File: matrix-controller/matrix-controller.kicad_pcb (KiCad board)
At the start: 2 copper layers, 1 part

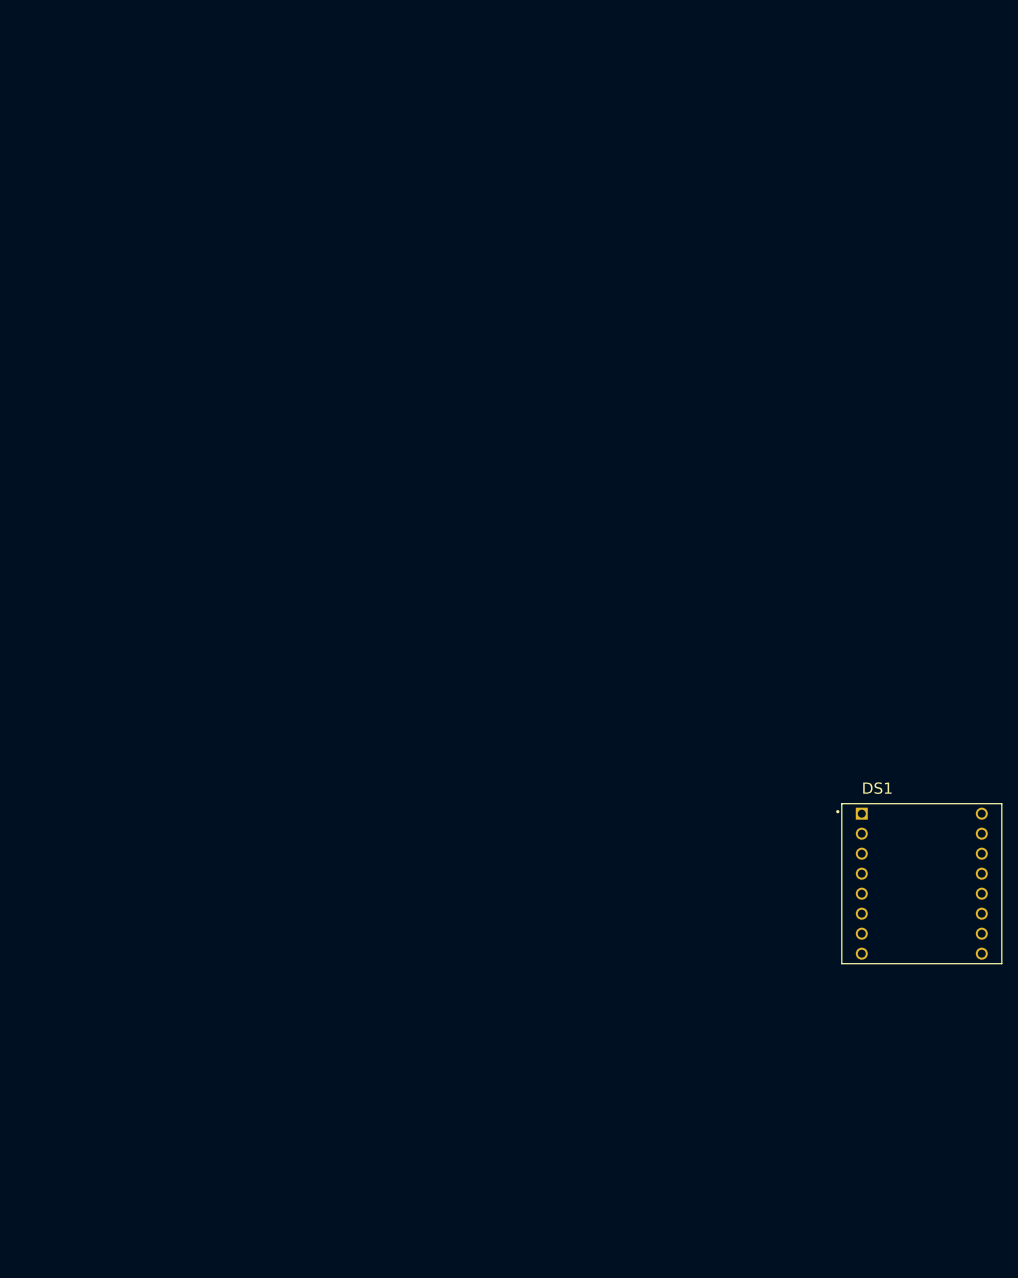
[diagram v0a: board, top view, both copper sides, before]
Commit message: Base of the schematic is done, need to add IMU and regulator and finish the rest of the panels
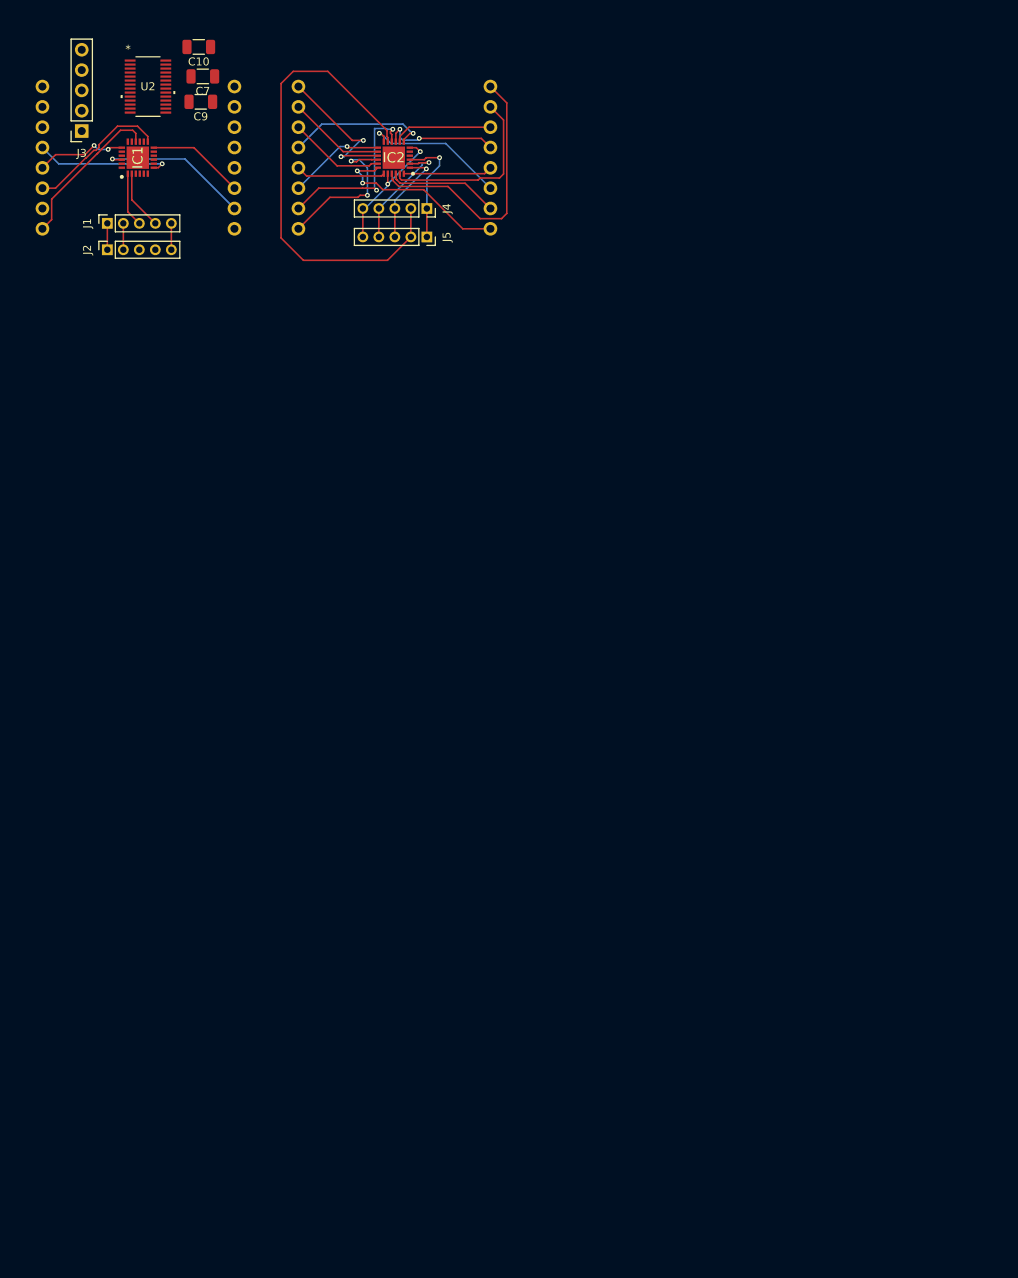
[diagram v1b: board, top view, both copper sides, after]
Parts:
- removed DS1: TA08-81GWA, TA08-81GWA:DISPLAY_TA08-81GWA
- added C10: 0.47uF, Capacitor_SMD:C_1206_3216Metric, F.Cu at (23.6, 2.16)
- added C7: 10uF, Capacitor_SMD:C_1206_3216Metric, F.Cu at (24.1, 5.84)
- added C9: 0.1uF, Capacitor_SMD:C_1206_3216Metric, F.Cu at (23.9, 9.02)
- added IC1: IS31FL3728-QFLS2-TR, IS31FL3728-QFLS2-TR:QFN50P400X400X80-25N-D, F.Cu at (16.0, 16.0)
- added IC2: IS31FL3728-QFLS2-TR, IS31FL3728-QFLS2-TR:QFN50P400X400X80-25N-D, F.Cu at (48.0, 16.0)
- added J1: 1x05_Socket_Front, Connector_PinSocket_2.00mm:PinSocket_1x05_P2.00mm_Vertical, F.Cu at (12.2, 24.2)
- added J2: 1x05_Socket_Back, Connector_PinSocket_2.00mm:PinSocket_1x05_P2.00mm_Vertical, F.Cu at (12.2, 27.5)
- added J3: Conn_01x05_Pin, Connector_PinSocket_2.54mm:PinSocket_1x05_P2.54mm_Vertical, F.Cu at (8.99, 12.7)
- added J4: 1x05_Socket_Front_Input, Connector_PinSocket_2.00mm:PinSocket_1x05_P2.00mm_Vertical, F.Cu at (52.1, 22.4)
- added J5: 1x05_Socket_Left, Connector_PinSocket_2.00mm:PinSocket_1x05_P2.00mm_Vertical, F.Cu at (52.1, 25.9)
- added U1: 1088BS, lib_fp:LED_1088, B.Cu at (32.0, 0.00)
- added U2: XMSM0G3507SDGS28R, footprints:VSSOP28_DGS_TEX, F.Cu at (17.3, 7.11)
- added U3: 1088BS, lib_fp:LED_1088, B.Cu at (64.0, 0.00)
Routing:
- net VCC: track 0.00 -> 63.1 mm
- net /MatrixPlusDriver1/C4: track 0.00 -> 34.2 mm
- net /MatrixPlusDriver1/C2: track 0.00 -> 23.0 mm
- net /MatrixPlusDriver1/C6: track 0.00 -> 22.9 mm, vias 0 -> 2
- net /MatrixPlusDriver1/R4: track 0.00 -> 22.8 mm, vias 0 -> 2
- net GND: track 0.00 -> 19.9 mm, vias 0 -> 2
- net /MatrixPlusDriver1/C8: track 0.00 -> 19.8 mm, vias 0 -> 2
- net /MatrixPlusDriver/C8: track 0.00 -> 19.5 mm
- net /MatrixPlusDriver1/R8: track 0.00 -> 19.2 mm, vias 0 -> 2
- net /MatrixPlusDriver/C3: track 0.00 -> 19.0 mm, vias 0 -> 1
- net /MatrixPlusDriver1/R5: track 0.00 -> 18.1 mm, vias 0 -> 1
- net /MatrixPlusDriver1/R1: track 0.00 -> 17.8 mm, vias 0 -> 1
- net /MatrixPlusDriver/R6: track 0.00 -> 17.8 mm
- net /MatrixPlusDriver/R1: track 0.00 -> 17.1 mm, vias 0 -> 1
- net SCL0_F: track 0.00 -> 14.8 mm, vias 0 -> 1
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
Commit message: Updates to pcb. Switched to 4 wire connecions. Added IMU and usb C port footprints
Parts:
- added IC3: IS31FL3728-QFLS2-TR, IS31FL3728-QFLS2-TR:QFN50P400X400X80-25N-D, F.Cu at (67.0, 151.6)
- added IC4: IS31FL3728-QFLS2-TR, IS31FL3728-QFLS2-TR:QFN50P400X400X80-25N-D, F.Cu at (67.0, 110.0)
- added IC5: IS31FL3728-QFLS2-TR, IS31FL3728-QFLS2-TR:QFN50P400X400X80-25N-D, F.Cu at (31.7, 151.6)
- added IC6: IS31FL3728-QFLS2-TR, IS31FL3728-QFLS2-TR:QFN50P400X400X80-25N-D, F.Cu at (31.7, 110.0)
- added J10: 1x05_SocketBack_Input, Connector_PinSocket_2.00mm:PinSocket_1x05_P2.00mm_Vertical, F.Cu at (113.3, 117.2)
- added J11: 1x05_Socket_Right, Connector_PinSocket_2.00mm:PinSocket_1x05_P2.00mm_Vertical, F.Cu at (117.4, 117.2)
- added J12: 1x05_Socket_Right_Input, Connector_PinSocket_2.00mm:PinSocket_1x05_P2.00mm_Vertical, F.Cu at (121.4, 117.2)
- added J6: 1x05_Socket_Left_Input, Connector_PinSocket_2.00mm:PinSocket_1x05_P2.00mm_Vertical, F.Cu at (101.2, 117.2)
- added J7: 1x05_Socket_Left, Connector_PinSocket_2.00mm:PinSocket_1x05_P2.00mm_Vertical, F.Cu at (105.2, 117.2)
- added J8: 1x05_Socket_Top_Input, Connector_PinSocket_2.00mm:PinSocket_1x05_P2.00mm_Vertical, F.Cu at (109.3, 117.2)
- added J9: Conn_01x04_Pin, Connector_Wire:SolderWire-0.25sqmm_1x04_P4.5mm_D0.65mm_OD2mm, F.Cu at (1.77, 1.52)
- added U4: 1088BS, lib_fp:LED_1088, F.Cu at (64.6, 115.9)
- added U5: 1088BS, lib_fp:LED_1088, F.Cu at (64.6, 74.3)
- added U6: 1088BS, lib_fp:LED_1088, F.Cu at (29.3, 115.9)
- added U7: 1088BS, lib_fp:LED_1088, F.Cu at (29.3, 74.3)
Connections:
- IC2 pad 3: SDB_F -> VCC
- IC2 pad 6: GND -> VCC
- J5 pad 1: SDB_F -> unconnected-(J5-Pin_1-Pad1)
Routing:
- net unconnected-(J5-Pin_1-Pad1): vias 0 -> 1
- net SDB_F: vias 1 -> 0
